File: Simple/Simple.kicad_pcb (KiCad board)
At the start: 2 copper layers, 33 parts, among them J6 Conn_01x02_Female, Q1 BSS138, Q2 BSS138, SW1 SW_Push

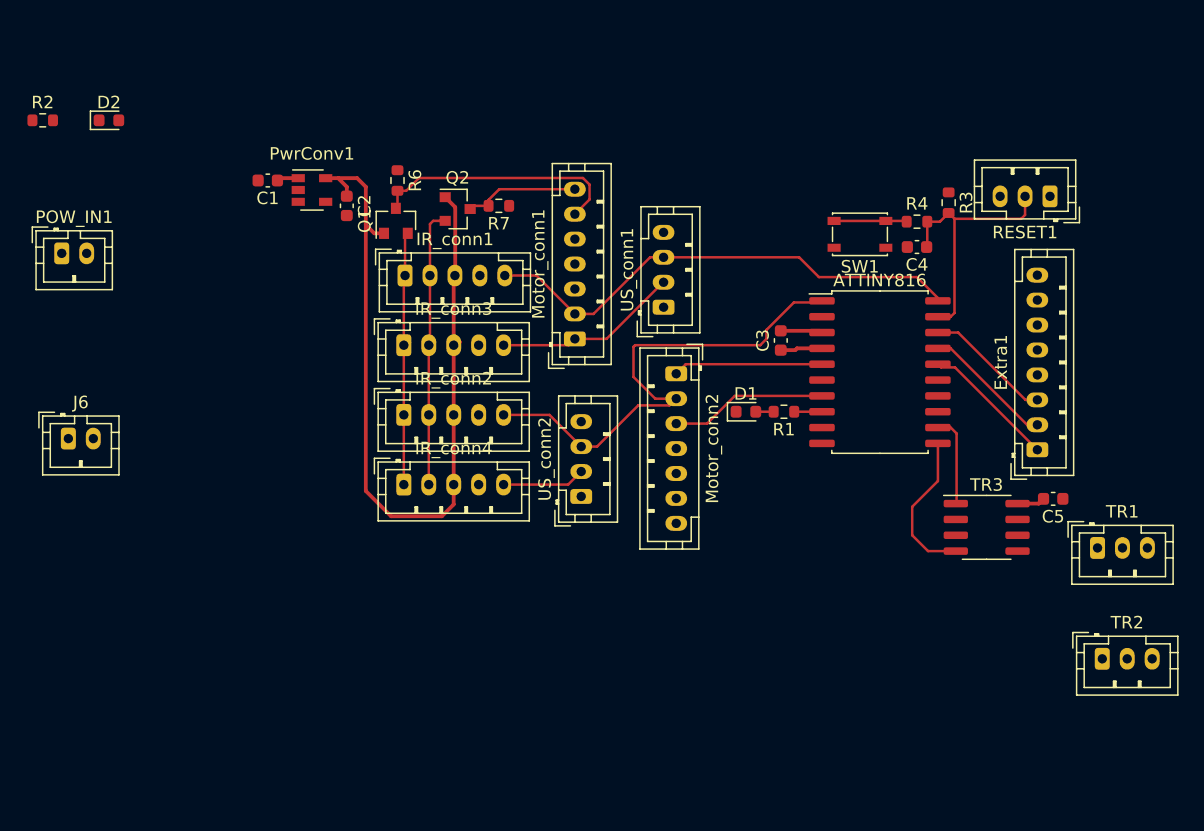
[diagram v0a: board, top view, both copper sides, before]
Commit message: rotated motor/ultrasonic connectors and added traces for all but pwr, gnd, d+/-
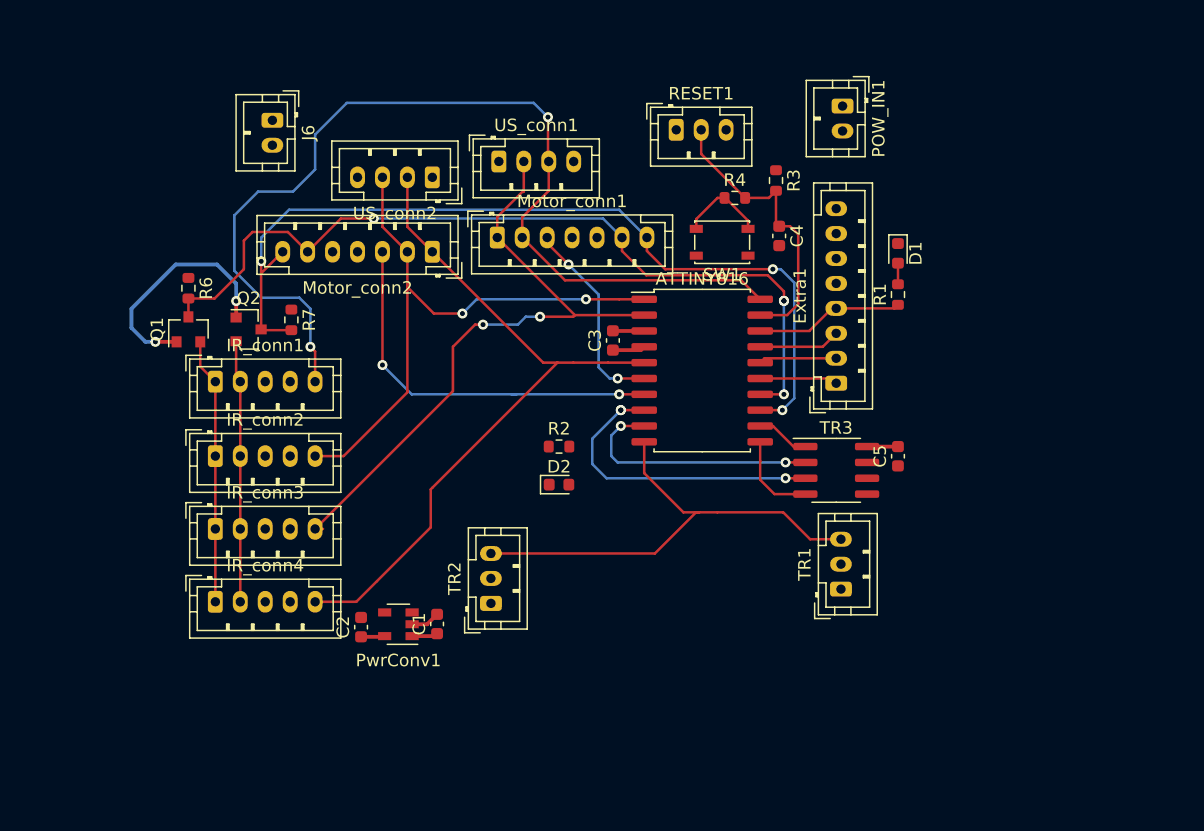
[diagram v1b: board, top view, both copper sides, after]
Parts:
- moved POW_IN1 63.7 mm to (166.8, 31.4), turned to 270 degrees
- moved TR2 49.2 mm to (138.6, 71.2), turned to 90 degrees
- moved R2 49.0 mm to (144.0, 58.7)
- moved D2 46.4 mm to (144.0, 61.7)
- moved C1 38.1 mm to (134.2, 72.9), turned to 90 degrees
- moved PwrConv1 35.5 mm to (131.1, 72.9), turned to 180 degrees
- moved C2 33.8 mm to (128.1, 73.2), turned to 90 degrees
- moved RESET1 30.4 mm to (153.4, 33.3), turned to 0 degrees
- moved J6 30.3 mm to (121.0, 32.5), turned to 270 degrees
- moved US_conn2 28.2 mm to (133.9, 37.1), turned to 180 degrees
- moved Motor_conn2 21.9 mm to (133.9, 43.1), turned to 180 degrees
- moved IR_conn3 21.1 mm to (116.5, 65.3)
- moved TR1 20.8 mm to (166.6, 70.1), turned to 90 degrees
- moved Q2 19.3 mm to (119.1, 49.3)
- moved R7 19.0 mm to (122.6, 48.5), turned to 270 degrees
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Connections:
- ATTINY816 pad 10: /~DataDirRead -> /Interrupt
- ATTINY816 pad 15: /Interrupt -> Net-(ATTINY816-Pad15)
- ATTINY816 pad 8: /PA7 -> /DataDirWrite
- ATTINY816 pad 9: /DataDirWrite -> /~DataDirRead
- Extra1 pad 1: Net-(ATTINY816-Pad16) -> Net-(ATTINY816-Pad15)
- Extra1 pad 2: Net-(ATTINY816-Pad17) -> Net-(ATTINY816-Pad16)
- Extra1 pad 3: Net-(ATTINY816-Pad18) -> Net-(ATTINY816-Pad17)
- Extra1 pad 4: /PA7 -> Net-(ATTINY816-Pad18)
- R1 pad 1: /PA7 -> Net-(ATTINY816-Pad18)
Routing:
- net /SDA: track 9.33 -> 71.4 mm, vias 0 -> 3
- net /SCL: track 20.4 -> 68.0 mm, vias 0 -> 4
- net +3V3: track 65.6 -> 20.8 mm, vias 0 -> 2
- net /ECHO1: track 40.1 -> 80.5 mm, vias 0 -> 2
- net /Interrupt: track 0.00 -> 38.6 mm
- net /Out4: track 18.7 -> 56.6 mm
- net /Out3: track 14.9 -> 52.1 mm, vias 0 -> 2
- net /DataDirWrite: track 0.00 -> 24.7 mm, vias 0 -> 3
- net /~DataDirRead: track 0.00 -> 20.4 mm, vias 0 -> 2
- net /DIR2: track 12.6 -> 31.4 mm, vias 0 -> 2
- net /DIR1: track 0.00 -> 16.1 mm, vias 0 -> 2
- net /ECHO2: track 40.1 -> 48.6 mm, vias 0 -> 2
- net Net-(ATTINY816-Pad15): track 0.00 -> 6.25 mm
- net Net-(ATTINY816-Pad16): track 10.8 -> 6.24 mm
- net /TXD: track 12.2 -> 8.12 mm
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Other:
- copper layers 2 -> 4

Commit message: minor routing changes and added pwr and gnd planes
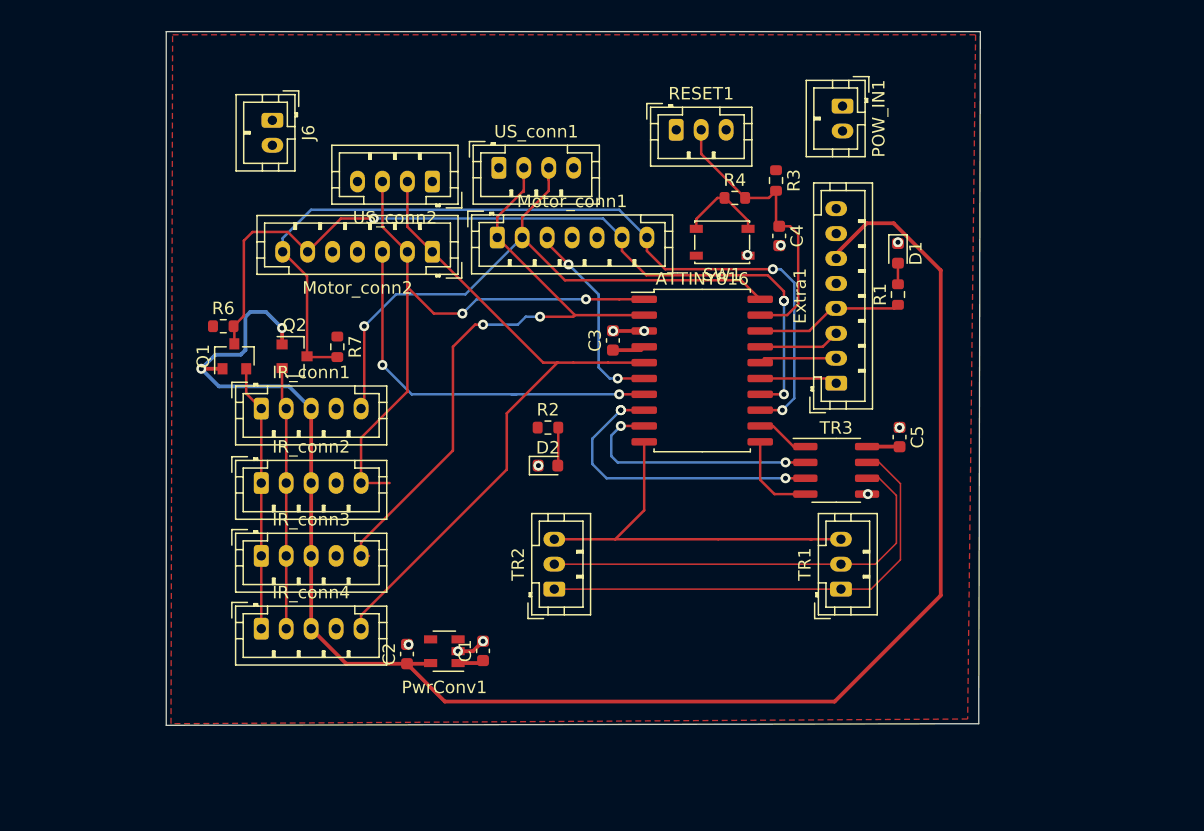
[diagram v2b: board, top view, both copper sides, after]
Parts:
- moved TR2 5.21 mm to (143.6, 70.1)
- moved Q1 4.27 mm to (118.0, 51.4)
- moved C1 4.27 mm to (137.9, 75.1)
- moved C2 4.27 mm to (131.8, 75.3)
- moved IR_conn1 4.27 mm to (120.1, 55.6)
- moved IR_conn2 4.27 mm to (120.1, 61.6)
- moved Q2 4.27 mm to (122.8, 51.4)
- moved R7 4.27 mm to (126.2, 50.7)
- moved IR_conn3 4.27 mm to (120.1, 67.4)
- moved IR_conn4 4.27 mm to (120.1, 73.3)
- moved PwrConv1 4.27 mm to (134.8, 75.1)
- moved R6 4.13 mm to (117.1, 49.0), turned to 0 degrees
- moved D2 1.76 mm to (143.1, 60.2)
- moved R2 1.76 mm to (143.1, 57.1)
- moved C5 1.54 mm to (171.3, 57.9), turned to 270 degrees
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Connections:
- TR1 pad 1: /D+ -> /D-
- TR1 pad 2: /D- -> /D+
- TR2 pad 1: /D+ -> /D-
- TR2 pad 2: /D- -> /D+
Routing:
- net +3V3: track 20.8 -> 137.0 mm
- net /D-: track 0.00 -> 38.2 mm
- net /D+: track 0.00 -> 34.9 mm
- net /ECHO1: track 80.5 -> 51.9 mm, vias 2 -> 1
- net /Interrupt: track 38.6 -> 31.9 mm
- net Net-(D2-Pad2): track 0.00 -> 3.06 mm
- net /ECHO2: track 48.6 -> 50.2 mm
- net /Out3: track 52.1 -> 53.6 mm
- net /Out4: track 56.6 -> 55.3 mm
- net /SDA: track 71.4 -> 70.4 mm, vias 3 -> 2
- net /SCL: track 68.0 -> 67.5 mm
- net GND: vias 0 -> 24
- added copper zone on F.Cu, net +5V
- added copper zone on In1.Cu, net GND
- added copper zone on In2.Cu, net GND
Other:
- board outline added: 65.3 x 55.6 mm
- net class 100 Ohm Diff Pair: trace_width 0.2032 -> 0.127
- rule trace_min: 0.2 -> 0.127

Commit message: added mounting holes and moved vias away from pads
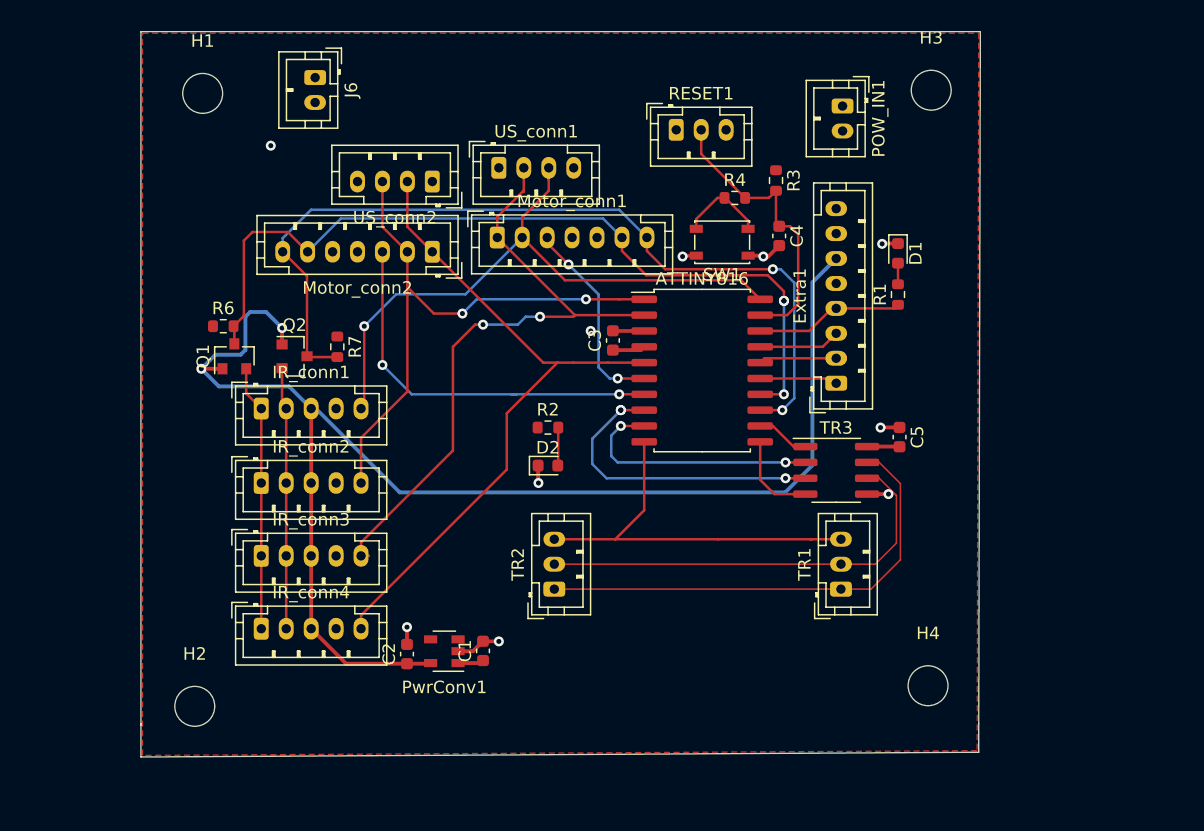
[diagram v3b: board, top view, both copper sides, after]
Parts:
- added H1: MountingHole, MountingHole:MountingHole_3.2mm_M3, F.Cu at (115.4, 30.4)
- added H2: MountingHole, MountingHole:MountingHole_3.2mm_M3, F.Cu at (114.8, 79.5)
- added H3: MountingHole, MountingHole:MountingHole_3.2mm_M3, F.Cu at (173.9, 30.1)
- added H4: MountingHole, MountingHole:MountingHole_3.2mm_M3, F.Cu at (173.6, 77.9)
- moved J6 4.85 mm to (124.5, 29.1)
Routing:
- net +3V3: track 137.0 -> 113.7 mm
- net GND: track 4.85 -> 17.4 mm, vias 24 -> 22
- net /ECHO2: track 50.2 -> 47.9 mm
- net /SCL: vias 4 -> 3
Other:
- board size 65.3 x 55.6 mm -> 67.3 x 58.2 mm

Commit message: Rerouted 3V3 trace and fixed borders of planes
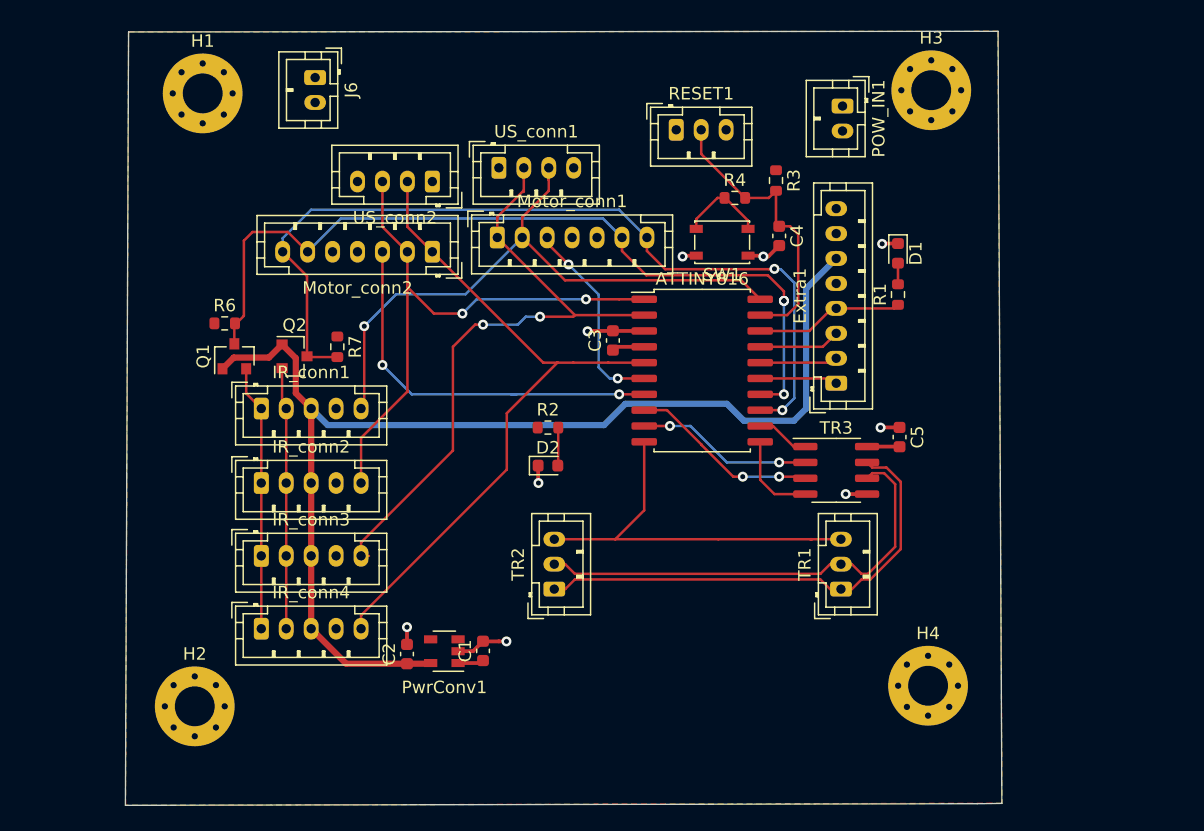
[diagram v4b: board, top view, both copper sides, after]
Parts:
- H1, H2, H3, H4: footprint MountingHole:MountingHole_3.2mm_M3 -> MountingHole:MountingHole_3.2mm_M3_Pad_Via
- moved R6 0.26 mm to (117.2, 48.8)
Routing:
- net +3V3: track 113.7 -> 95.4 mm, vias 2 -> 0
- net /DataDirWrite: track 24.7 -> 15.2 mm, vias 3 -> 2
- net /~DataDirRead: track 20.4 -> 14.1 mm
- net GND: track 17.4 -> 19.8 mm, vias 22 -> 9
- net /D+: track 34.9 -> 37.0 mm
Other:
- board size 67.3 x 58.2 mm -> 70.3 x 62.1 mm
- net class 3V3 Power added: clearance 0.2, trace_width 0.5, via_dia 0.8, via_drill 0.4

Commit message: fixed outline's right angles and moved silk lettering
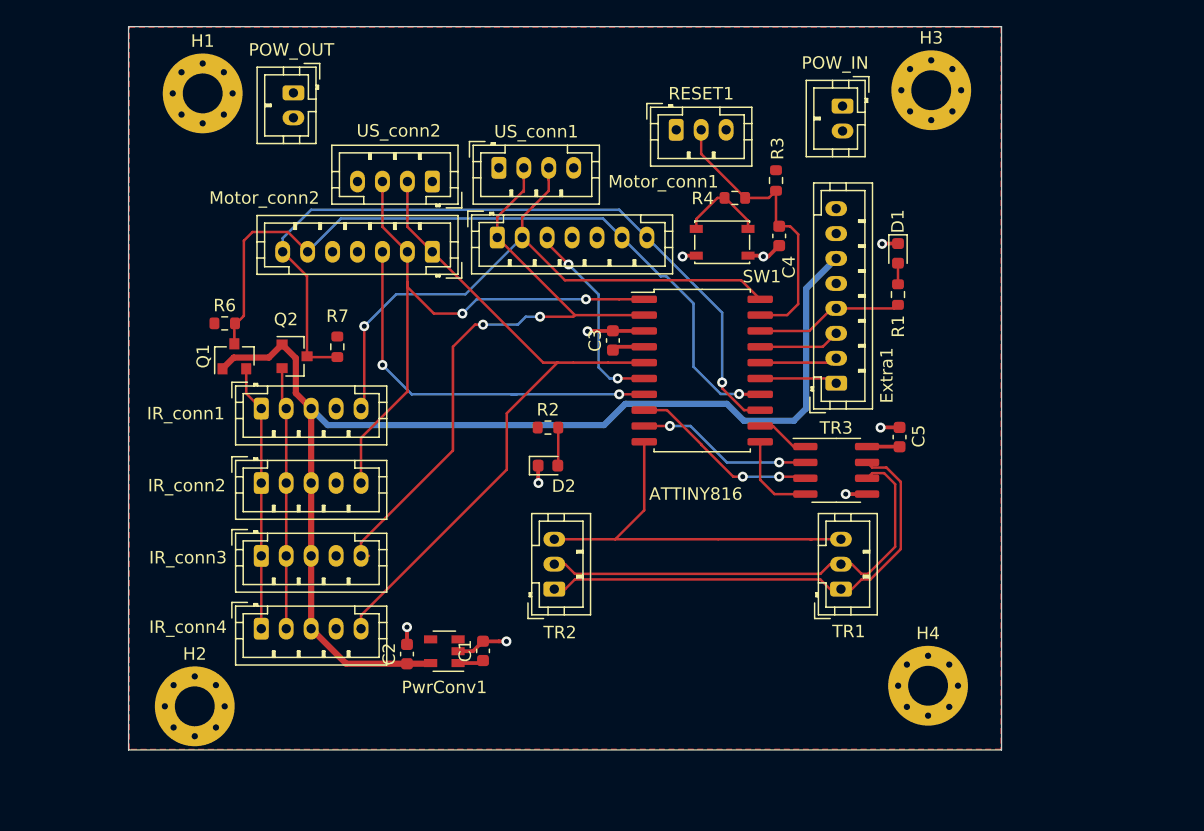
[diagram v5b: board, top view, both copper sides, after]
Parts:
- moved POW_OUT 2.13 mm to (122.7, 30.3)
- renumbered POW_IN1 to POW_IN, J6 to POW_OUT
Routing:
- net /SDA: track 70.4 -> 62.2 mm, vias 2 -> 1
- net /SCL: track 67.5 -> 62.4 mm, vias 3 -> 1
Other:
- board size 70.3 x 62.1 mm -> 70 x 58 mm

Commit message: Modifications from review of PCB.
- Aligned connector and hole footprints
- Shifted positions of some bits of silkscreen text
- Redrew 3V3 connection to utility connection
- Added 5V connection on backplane to microcontroller
- Added PCB version and manufacturer serial number silkscreen text
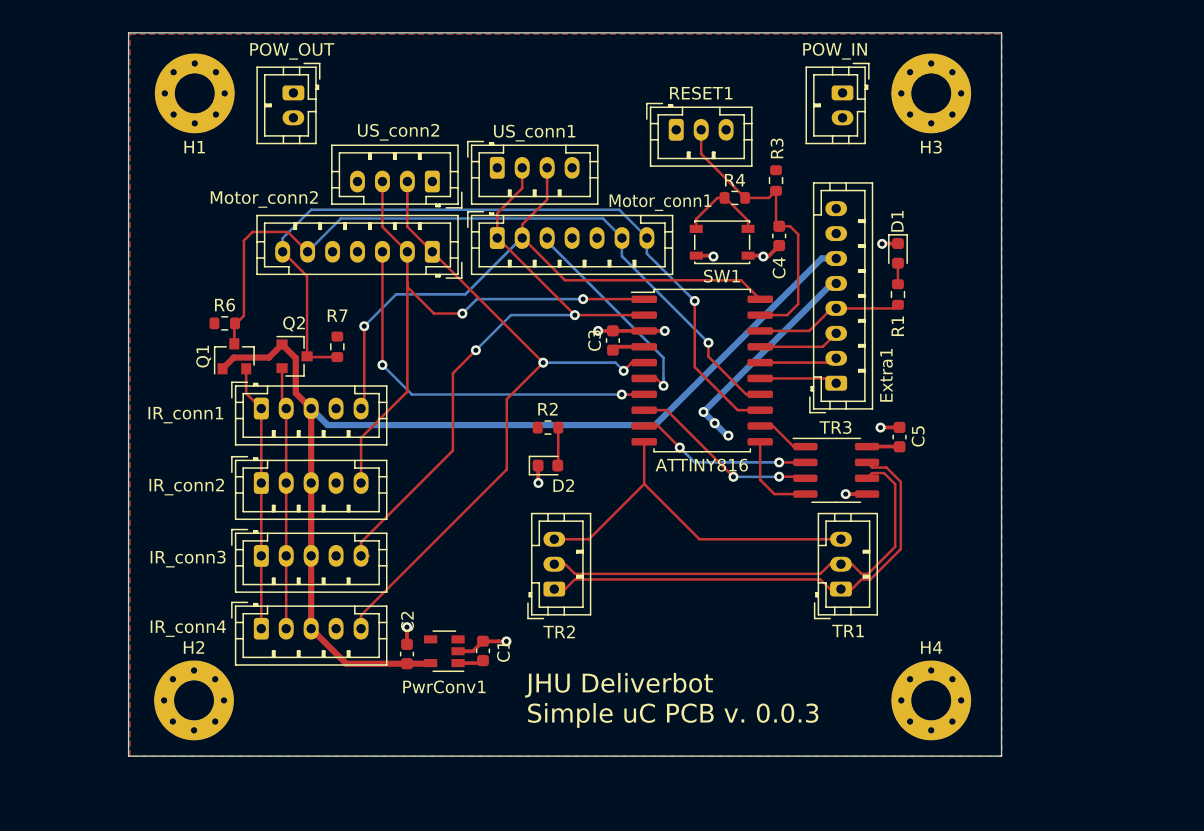
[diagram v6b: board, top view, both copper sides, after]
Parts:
- moved H4 1.20 mm to (173.9, 79.0)
- moved POW_IN 1.06 mm to (166.8, 30.3)
- moved H1 0.63 mm to (114.8, 30.4)
- moved H2 0.48 mm to (114.8, 79.0)
- moved H3 0.25 mm to (173.9, 30.4)
- moved US_conn1 0.13 mm to (139.1, 36.3)
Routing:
- net +5V: track 7.32 -> 25.0 mm, vias 0 -> 3
- net +3V3: track 95.4 -> 88.7 mm
- net /Out3: track 53.6 -> 50.9 mm
- net /SCL: track 62.4 -> 59.7 mm
- net /Interrupt: track 31.9 -> 30.0 mm
- net /DIR1: track 16.1 -> 18.0 mm, vias 2 -> 1
- net /ECHO1: track 51.9 -> 50.4 mm
- net GND: track 19.8 -> 21.2 mm, vias 9 -> 10
- net /Out4: track 55.3 -> 55.4 mm, vias 0 -> 2
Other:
- board text added: "JHU Deliverbot Simple uC PCB v. 0.0.3"
- board text added: "JLCJLCJLCJLC"

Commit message: Rerouted differential pair traces with dimensions for 120 ohm diff. imped.
Diff. trace width changed to 0.126238 mm (4.97 mil); separation changed to
0.2032 mm (8 mil).  Min. trace width in global design rules changed to
0.09 mm (3.5 mil), which is JLCPCB's min. trace width for traces on the
**outer layer** of 1 oz Cu. 4- or 6-layer boards.  (Note that min. trace
width for inner layers is still 0.127 mm (5 mil).
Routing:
- net GND: track 21.2 -> 21.7 mm, vias 10 -> 11
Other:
- net class 100 Ohm Diff Pair: trace_width 0.127 -> 0.126238
- rule trace_min: 0.127 -> 0.09

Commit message: Added note to Dwgs.User layer in PCB indicating which JLCPCB stackup to use to get proper 120-ohm diff. imped. control.
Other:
- board text added: "Use JLC7628 stackup w. 4 layers, 1 oz copper, 1.6 mm board thickness to get 120 ohm differen. imped. on D+/- serial traces."
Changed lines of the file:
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@@
   (general
     (thickness 1.6)
-    (drawings 6)
+    (drawings 7)
     (tracks 281)
     (zones 0)
@@
     (46 B.CrtYd user)
     (47 F.CrtYd user)
-    (49 F.Fab user)
+    (49 F.Fab user hide)
   )
   (setup
@@
     )
   )
+  (gr_text "Use JLC7628 stackup w. 4 layers, \n1 oz copper, 1.6 mm board thickness\nto get 120 ohm differen. imped. on \nD+/- serial traces." (at 156.2 75.65) (layer Dwgs.User)
+    (effects (font (size 1 1) (thickness 0.15)))
+  )
   (gr_text JLCJLCJLCJLC (at 124.15 80.75) (layer B.SilkS)
